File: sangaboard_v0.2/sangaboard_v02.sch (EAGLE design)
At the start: 18 parts, among them IC1 ULN2003A, IC2 ULN2003A

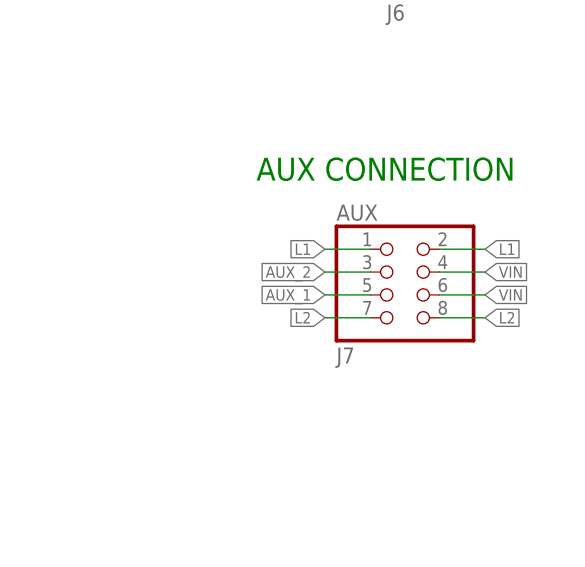
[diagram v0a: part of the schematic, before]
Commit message: Updated Bottom Layer
Have updated the Aux header pin connection to Ground.
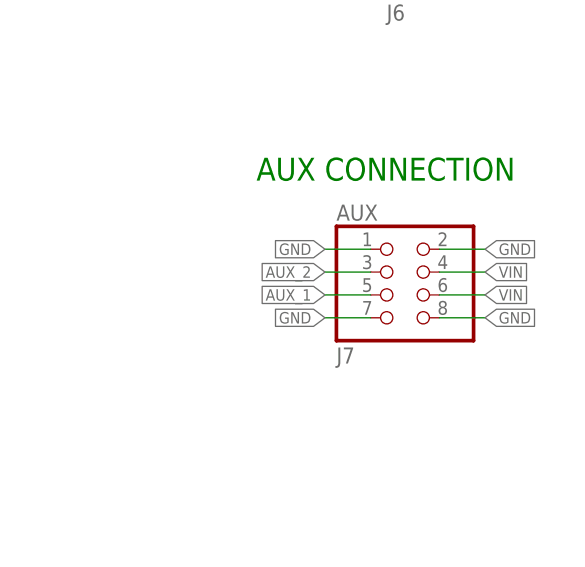
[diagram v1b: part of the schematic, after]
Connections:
- removed net L1: AUX.1, AUX.2
- removed net L2: AUX.7, AUX.8
- net GND: now also AUX.1, AUX.2, AUX.7, AUX.8
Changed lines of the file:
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@@
 <?xml version="1.0" encoding="utf-8"?>
 <!DOCTYPE eagle SYSTEM "eagle.dtd">
-<eagle version="8.5.2">
+<eagle version="9.0.0">
 <drawing>
 <settings>
@@
 <wire x1="-119.38" y1="25.4" x2="-119.38" y2="30.48" width="0.1524" layer="91"/>
 </segment>
+<segment>
+<pinref part="AUX" gate="A" pin="1"/>
+<wire x1="5.08" y1="66.04" x2="0" y2="66.04" width="0.1524" layer="91"/>
+<label x="0" y="66.04" size="1.27" layer="95" ratio="6" rot="R180" xref="yes"/>
+</segment>
+<segment>
+<pinref part="AUX" gate="A" pin="7"/>
+<wire x1="5.08" y1="58.42" x2="0" y2="58.42" width="0.1524" layer="91"/>
+<label x="0" y="58.42" size="1.27" layer="95" ratio="6" rot="R180" xref="yes"/>
+</segment>
+<segment>
+<pinref part="AUX" gate="A" pin="2"/>
+<wire x1="12.7" y1="66.04" x2="17.78" y2="66.04" width="0.1524" layer="91"/>
+<label x="17.78" y="66.04" size="1.27" layer="95" ratio="6" xref="yes"/>
+</segment>
+<segment>
+<pinref part="AUX" gate="A" pin="8"/>
+<wire x1="12.7" y1="58.42" x2="17.78" y2="58.42" width="0.1524" layer="91"/>
+<label x="17.78" y="58.42" size="1.27" layer="95" ratio="6" xref="yes"/>
+</segment>
 </net>
 <net name="VIN" class="0">
@@
 </segment>
 </net>
-<net name="L1" class="0">
-<segment>
-<pinref part="AUX" gate="A" pin="1"/>
-<wire x1="5.08" y1="66.04" x2="0" y2="66.04" width="0.1524" layer="91"/>
-<label x="0" y="66.04" size="1.27" layer="95" ratio="6" rot="R180" xref="yes"/>
-</segment>
-<segment>
-<pinref part="AUX" gate="A" pin="2"/>
-<wire x1="12.7" y1="66.04" x2="17.78" y2="66.04" width="0.1524" layer="91"/>
-<label x="17.78" y="66.04" size="1.27" layer="95" ratio="6" xref="yes"/>
-</segment>
-</net>
-<net name="L2" class="0">
-<segment>
-<pinref part="AUX" gate="A" pin="7"/>
-<wire x1="5.08" y1="58.42" x2="0" y2="58.42" width="0.1524" layer="91"/>
-<label x="0" y="58.42" size="1.27" layer="95" ratio="6" rot="R180" xref="yes"/>
-</segment>
-<segment>
-<pinref part="AUX" gate="A" pin="8"/>
-<wire x1="12.7" y1="58.42" x2="17.78" y2="58.42" width="0.1524" layer="91"/>
-<label x="17.78" y="58.42" size="1.27" layer="95" ratio="6" xref="yes"/>
-</segment>
-</net>
